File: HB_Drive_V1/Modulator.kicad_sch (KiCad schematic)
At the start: 0 parts

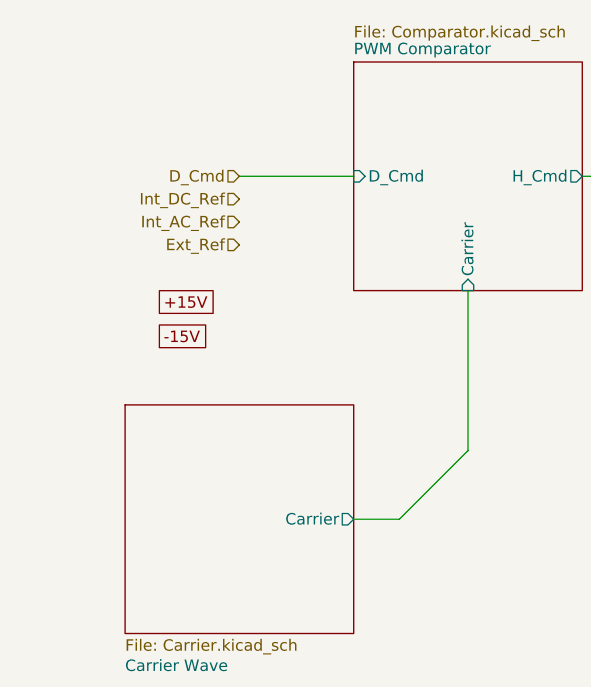
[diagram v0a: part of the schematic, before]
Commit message: Adds Carrier Wave Circuit and Comparator Circuit
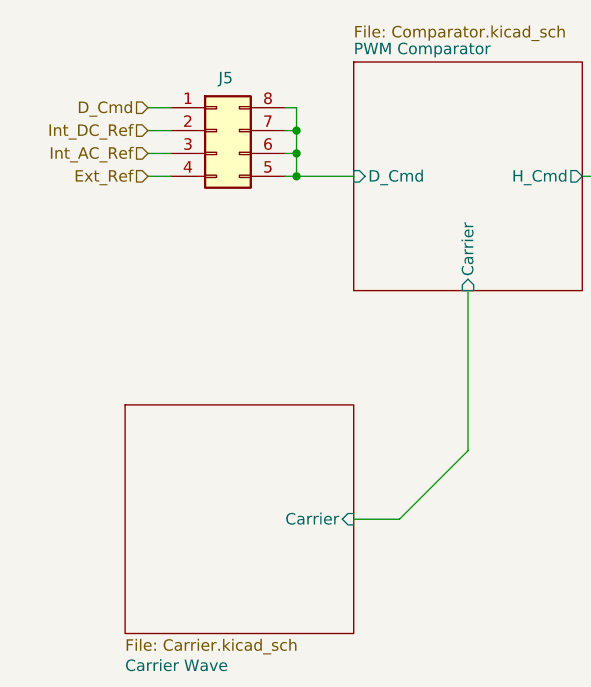
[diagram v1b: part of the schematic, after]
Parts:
- added J5: Conn_02x04_Counter_Clockwise, Connector_PinSocket_1.27mm:PinSocket_2x04_P1.27mm_Vertical, symbol Connector_Generic:Conn_02x04_Counter_Clockwise
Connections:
- net D_Cmd: now also J5.1 (Pin_1)
- net Ext_Ref: now also J5.4 (Pin_4)
- net Int_AC_Ref: now also J5.3 (Pin_3)
- net Int_DC_Ref: now also J5.2 (Pin_2)
- new net PWM Comparator/D_Cmd: J5.5 (Pin_5), J5.6 (Pin_6), J5.7 (Pin_7), J5.8 (Pin_8)
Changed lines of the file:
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@@
 	(generator_version "10.0")
 	(paper "A4")
+	(junction
+		(at 95.25 73.66)
+		(diameter 0)
+		(color 0 0 0 0)
+	)
+	(junction
+		(at 95.25 76.2)
+		(diameter 0)
+		(color 0 0 0 0)
+	)
+	(junction
+		(at 95.25 71.12)
+		(diameter 0)
+		(color 0 0 0 0)
+	)
+	(wire
+		(pts
+			(xy 78.74 71.12) (xy 81.28 71.12)
+		)
+		(stroke
+			(width 0)
+			(type default)
+		)
+	)
 	(wire
 		(pts
@@
 	(wire
 		(pts
-			(xy 88.9 76.2) (xy 101.6 76.2)
-		)
-		(stroke
-			(width 0)
-			(type default)
-		)
-	)
-	(wire
-		(pts
 			(xy 106.68 114.3) (xy 114.3 106.68)
 		)
@@
 	(wire
 		(pts
+			(xy 95.25 68.58) (xy 95.25 71.12)
+		)
+		(stroke
+			(width 0)
+			(type default)
+		)
+	)
+	(wire
+		(pts
+			(xy 78.74 76.2) (xy 81.28 76.2)
+		)
+		(stroke
+			(width 0)
+			(type default)
+		)
+	)
+	(wire
+		(pts
+			(xy 95.25 76.2) (xy 93.98 76.2)
+		)
+		(stroke
+			(width 0)
+			(type default)
+		)
+	)
+	(wire
+		(pts
+			(xy 95.25 76.2) (xy 101.6 76.2)
+		)
+		(stroke
+			(width 0)
+			(type default)
+		)
+	)
+	(wire
+		(pts
+			(xy 95.25 71.12) (xy 93.98 71.12)
+		)
+		(stroke
+			(width 0)
+			(type default)
+		)
+	)
+	(wire
+		(pts
 			(xy 215.9 74.93) (xy 228.6 74.93)
 		)
@@
 	(wire
 		(pts
+			(xy 78.74 68.58) (xy 81.28 68.58)
+		)
+		(stroke
+			(width 0)
+			(type default)
+		)
+	)
+	(wire
+		(pts
 			(xy 165.1 77.47) (xy 177.8 77.47)
 		)
@@
 	(wire
 		(pts
+			(xy 78.74 73.66) (xy 81.28 73.66)
+		)
+		(stroke
+			(width 0)
+			(type default)
+		)
+	)
+	(wire
+		(pts
+			(xy 95.25 73.66) (xy 95.25 76.2)
+		)
+		(stroke
+			(width 0)
+			(type default)
+		)
+	)
+	(wire
+		(pts
+			(xy 95.25 71.12) (xy 95.25 73.66)
+		)
+		(stroke
+			(width 0)
+			(type default)
+		)
+	)
+	(wire
+		(pts
+			(xy 95.25 68.58) (xy 93.98 68.58)
+		)
+		(stroke
+			(width 0)
+			(type default)
+		)
+	)
+	(wire
+		(pts
 			(xy 101.6 114.3) (xy 106.68 114.3)
 		)
@@
 		)
 	)
-	(global_label "-15V"
-		(shape passive)
-		(at 80.01 93.98 0)
-		(fields_autoplaced yes)
-		(effects
-			(font
-				(size 1.27 1.27)
-			)
-			(justify left)
-		)
-		(property "Intersheetrefs" "${INTERSHEET_REFS}"
-			(at 86.9639 93.98 0)
-			(hide yes)
-			(show_name no)
-			(do_not_autoplace no)
-			(effects
-				(font
-					(size 1.27 1.27)
-				)
-				(justify left)
-			)
-		)
-	)
-	(global_label "+15V"
-		(shape passive)
-		(at 80.01 90.17 0)
-		(fields_autoplaced yes)
-		(effects
-			(font
-				(size 1.27 1.27)
-			)
-			(justify left)
-		)
-		(property "Intersheetrefs" "${INTERSHEET_REFS}"
-			(at 86.9639 90.17 0)
-			(hide yes)
-			(show_name no)
-			(do_not_autoplace no)
-			(effects
-				(font
-					(size 1.27 1.27)
-				)
-				(justify left)
-			)
-		)
-	)
-	(hierarchical_label "Ext_Ref"
+	(wire
+		(pts
+			(xy 95.25 73.66) (xy 93.98 73.66)
+		)
+		(stroke
+			(width 0)
+			(type default)
+		)
+	)
+	(hierarchical_label "D_Cmd"
 		(shape input)
-		(at 88.9 83.82 180)
+		(at 78.74 68.58 180)
+		(effects
+			(font
+				(size 1.27 1.27)
+			)
+			(justify right)
+		)
+	)
+	(hierarchical_label "Int_DC_Ref"
+		(shape input)
+		(at 78.74 71.12 180)
 		(effects
 			(font
@@
 		)
 	)
-	(hierarchical_label "Int_DC_Ref"
-		(shape input)
-		(at 88.9 78.74 180)
-		(effects
-			(font
-				(size 1.27 1.27)
-			)
-			(justify right)
-		)
-	)
 	(hierarchical_label "Int_AC_Ref"
 		(shape input)
-		(at 88.9 81.28 180)
+		(at 78.74 73.66 180)
 		(effects
 			(font
@@
 		)
 	)
-	(hierarchical_label "D_Cmd"
+	(hierarchical_label "Ext_Ref"
 		(shape input)
-		(at 88.9 76.2 180)
+		(at 78.74 76.2 180)
 		(effects
 			(font
@@
 			)
 			(justify right)
+		)
+	)
+	(symbol
+		(lib_id "Connector_Generic:Conn_02x04_Counter_Clockwise")
+		(at 86.36 71.12 0)
+		(unit 1)
+		(body_style 1)
+		(exclude_from_sim no)
+		(in_bom yes)
+		(on_board yes)
+		(in_pos_files yes)
+		(dnp no)
+		(property "Reference" "J5"
+			(at 87.376 65.278 0)
+			(show_name no)
+			(do_not_autoplace no)
+			(effects
+				(font
+					(size 1.27 1.27)
+				)
+			)
+		)
+		(property "Value" "Conn_02x04_Counter_Clockwise"
+			(at 87.63 64.77 0)
+			(hide yes)
+			(show_name no)
+			(do_not_autoplace no)
+			(effects
+				(font
+					(size 1.27 1.27)
+				)
+			)
+		)
+		(property "Footprint" "Connector_PinSocket_1.27mm:PinSocket_2x04_P1.27mm_Vertical"
+			(at 86.36 71.12 0)
+			(hide yes)
+			(show_name no)
+			(do_not_autoplace no)
+			(effects
+				(font
+					(size 1.27 1.27)
+				)
+			)
+		)
+		(property "Datasheet" ""
+			(at 86.36 71.12 0)
+			(hide yes)
+			(show_name no)
+			(do_not_autoplace no)
+			(effects
+				(font
+					(size 1.27 1.27)
+				)
+			)
+		)
+		(property "Description" "Generic connector, double row, 02x04, counter clockwise pin numbering scheme (similar to DIP package numbering), script generated (kicad-library-utils/schlib/autogen/connector/)"
+			(at 86.36 71.12 0)
+			(hide yes)
+			(show_name no)
+			(do_not_autoplace no)
+			(effects
+				(font
+					(size 1.27 1.27)
+				)
+			)
+		)
+		(pin "7"
+		)
+		(pin "5"
+		)
+		(pin "3"
+		)
+		(pin "6"
+		)
+		(pin "2"
+		)
+		(pin "1"
+		)
+		(pin "8"
+		)
+		(pin "4"
+		)
+		(instances
+			(project "HB_Drive_V1"
+				(path "/a9b54c89-4c8e-4c90-8a0d-ec2009e369b7/28e2d9d3-ebce-4623-8c7e-52f93025d826"
+					(reference "J5")
+					(unit 1)
+				)
+			)
 		)
 	)
@@
 			)
 		)
-		(pin "Carrier" output
+		(pin "Carrier" input
 			(at 101.6 114.3 0)
 			(effects

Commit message: Notes from conversation PF + MS
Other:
- note added: "Add adjustability to 555 timer period - target is factor of 10 freq, 10 kHz to 100 kHz"
- note added: "Change sheet name to "Protection""
- note added: "add deadtime circit with potentiometer"
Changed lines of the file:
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@@
 	(generator_version "10.0")
 	(paper "A4")
+	(text "Add adjustability to 555 timer period - target is factor of 10 freq, 10 kHz to 100 kHz\n"
+		(exclude_from_sim no)
+		(at 116.332 134.874 0)
+		(effects
+			(font
+				(size 1.27 1.27)
+			)
+		)
+	)
+	(text "Change sheet name to \"Protection\"\n"
+		(exclude_from_sim no)
+		(at 195.834 83.82 0)
+		(effects
+			(font
+				(size 1.27 1.27)
+			)
+		)
+	)
+	(text "add deadtime circit with potentiometer"
+		(exclude_from_sim no)
+		(at 152.4 93.98 0)
+		(effects
+			(font
+				(size 1.27 1.27)
+			)
+		)
+	)
 	(junction
 		(at 95.25 73.66)
@@
 			)
 		)
-		(pin "Carrier" input
+		(pin "Carrier" output
 			(at 101.6 114.3 0)
 			(effects
@@
 		(on_board yes)
 		(dnp no)
-		(fields_autoplaced yes)
 		(stroke
 			(width 0.1524)
@@
 		)
 		(property "Sheetfile" "CurrentMonitor.kicad_sch"
-			(at 177.8 89.4846 0)
-			(show_name no)
-			(do_not_autoplace no)
+			(at 177.8 59.182 0)
+			(show_name no)
+			(do_not_autoplace no)

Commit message: adds 10v reference and DC offsets / gain control to I_fdbk and V_fdbk
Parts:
- renumbered J5 to J7
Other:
- removed sheet Current Monitor
- added sheet Protection (Protection.kicad_sch)
- note removed: "Change sheet name to "Protection""
- note removed: "add deadtime circit with potentiometer"
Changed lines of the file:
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@@
-		)
-	)
-	(text "Change sheet name to \"Protection\"\n"
-		(exclude_from_sim no)
-		(at 195.834 83.82 0)
-		(effects
-			(font
-				(size 1.27 1.27)
-			)
-		)
-	)
-	(text "add deadtime circit with potentiometer"
-		(exclude_from_sim no)
-		(at 152.4 93.98 0)
-		(effects
-			(font
-				(size 1.27 1.27)
-			)
 		)
 	)
@@
 	(wire
 		(pts
-			(xy 215.9 74.93) (xy 228.6 74.93)
+			(xy 217.17 74.93) (xy 222.25 74.93)
 		)
 		(stroke
@@
 	(wire
 		(pts
-			(xy 215.9 77.47) (xy 228.6 77.47)
+			(xy 217.17 77.47) (xy 222.25 77.47)
 		)
 		(stroke
@@
 	(hierarchical_label "G_Lower_Cmd"
 		(shape output)
-		(at 228.6 77.47 0)
+		(at 222.25 77.47 0)
 		(effects
 			(font
@@
 	(hierarchical_label "G_Upper_Cmd"
 		(shape output)
-		(at 228.6 74.93 0)
+		(at 222.25 74.93 0)
 		(effects
 			(font
@@
 		(in_pos_files yes)
 		(dnp no)
-		(property "Reference" "J5"
+		(property "Reference" "J7"
 			(at 87.376 65.278 0)
 			(show_name no)
@@
 			(project "HB_Drive_V1"
 				(path "/a9b54c89-4c8e-4c90-8a0d-ec2009e369b7/28e2d9d3-ebce-4623-8c7e-52f93025d826"
-					(reference "J5")
+					(reference "J7")
 					(unit 1)
 				)
@@
 	(sheet
 		(at 177.8 63.5)
-		(size 38.1 25.4)
+		(size 39.37 26.67)
 		(exclude_from_sim no)
 		(in_bom yes)
 		(on_board yes)
 		(dnp no)
+		(fields_autoplaced yes)
 		(stroke
 			(width 0.1524)
@@
 			(color 0 0 0 0)
 		)
-		(property "Sheetname" "Current Monitor"
+		(property "Sheetname" "Protection"
 			(at 177.8 62.7884 0)
 			(show_name no)
@@
 			)
 		)
-		(property "Sheetfile" "CurrentMonitor.kicad_sch"
-			(at 177.8 59.182 0)
+		(property "Sheetfile" "Protection.kicad_sch"
+			(at 177.8 90.7546 0)
 			(show_name no)
 			(do_not_autoplace no)
@@
 				)
 				(justify left top)
+			)
+		)
+		(pin "+10V_Ref" input
+			(at 177.8 80.01 180)
+			(effects
+				(font
+					(size 1.27 1.27)
+				)
+				(justify left)
 			)
 		)
@@
 		)
 		(pin "G_Lower_Cmd_Out" output
-			(at 215.9 77.47 0)
+			(at 217.17 77.47 0)
 			(effects
 				(font
@@
 		)
 		(pin "G_Upper_Cmd_Out" output
-			(at 215.9 74.93 0)
+			(at 217.17 74.93 0)
 			(effects
 				(font
@@
 			(project "HB_Drive_V1"
 				(path "/a9b54c89-4c8e-4c90-8a0d-ec2009e369b7/28e2d9d3-ebce-4623-8c7e-52f93025d826"
-					(page "4")
-				)
-			)
+					(page "7")
+				)
+			)
